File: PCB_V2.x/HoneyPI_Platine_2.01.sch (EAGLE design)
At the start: 69 parts

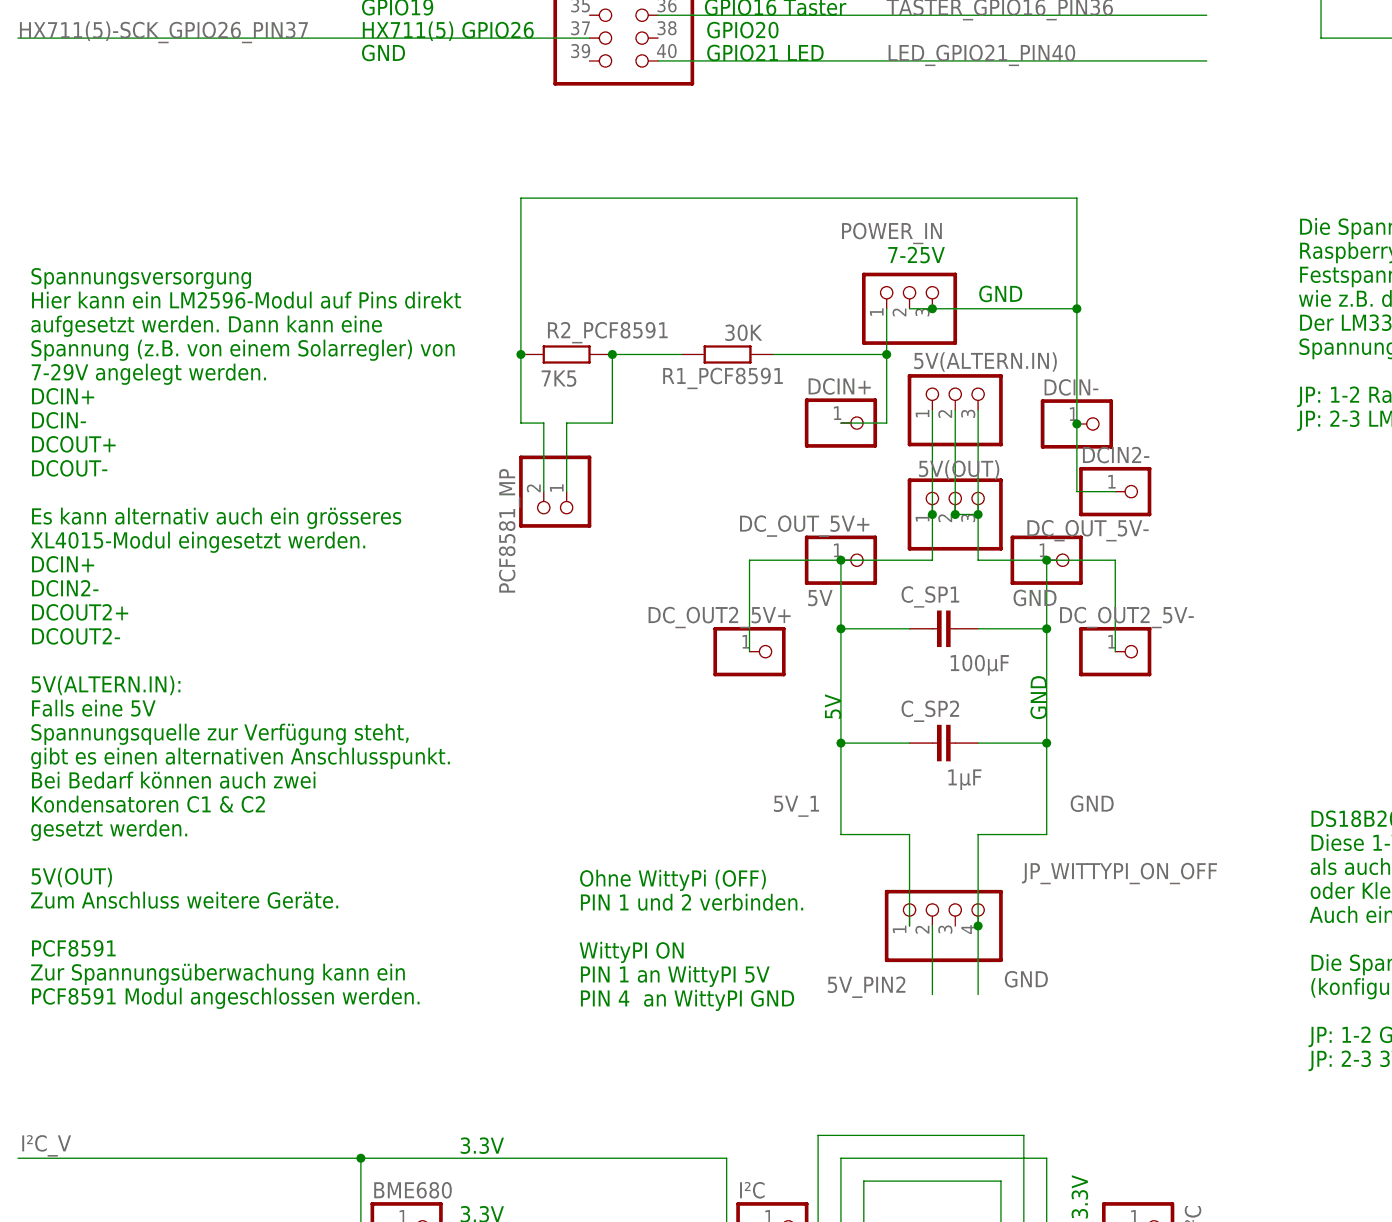
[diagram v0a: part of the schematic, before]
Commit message: 2x Polyfuse
The circuit has been extended by 2 optional polyfuses or similar.  The fuse size has been accepted and not yet verified.
Please note: The operator of the board must ensure safe operation. Accordingly, a fuse must be installed in accordance with the regulations.
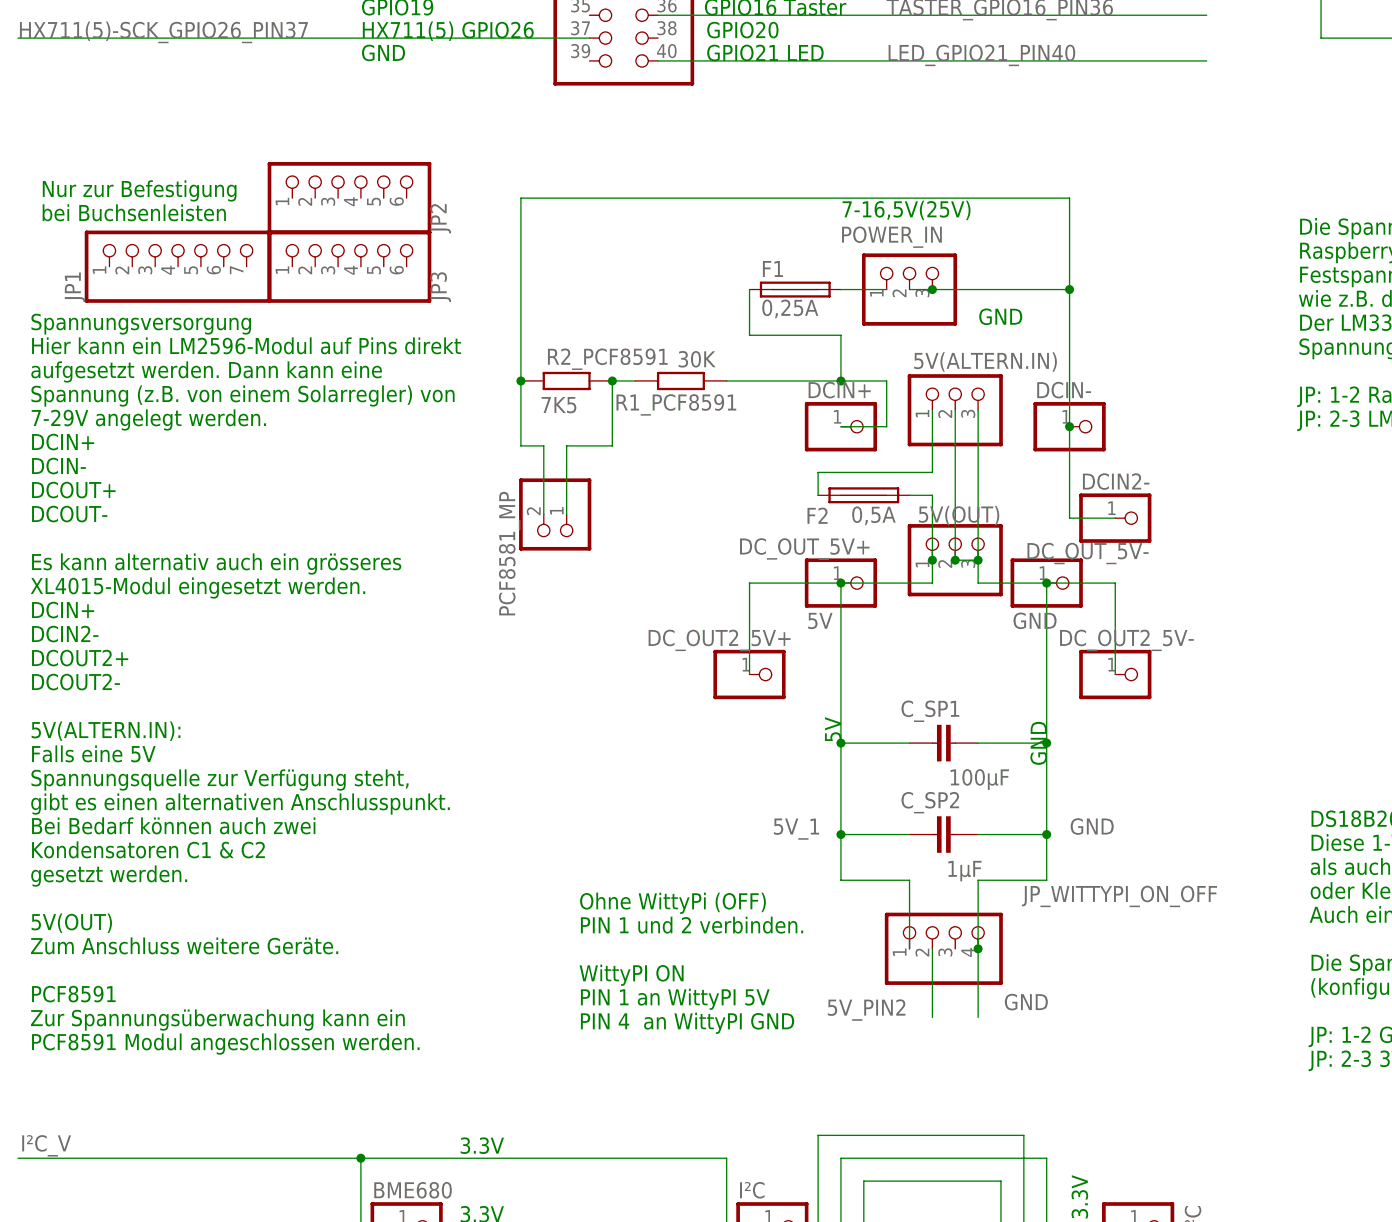
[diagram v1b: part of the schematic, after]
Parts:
- added F1: 0,25A, fuse:TR5
- added F2: 0,5A, fuse:TR5
- added JP1: (no value), pinhead:PINHD-1X7
- added JP2, JP3: (no value), pinhead:PINHD-1X6
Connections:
- removed net N$45: DCIN+.1, POWER_IN.1, R1_PCF8591.1
- new net N$5: DCIN+.1, F1.1, R1_PCF8591.1
- new net N$7: F1.2, POWER_IN.1
- new net N$9: 5V(ALTERN.IN).1, F2.2
- net 5V_1: now also F2.1; no longer 5V(ALTERN.IN).1
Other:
- note added: "7-16,5V(25V)"
- note added: "Nur zur Befestigung bei Buchsenleisten"
- note removed: "7-25V"
- moved on the sheet: 5V(OUT), C_SP1, C_SP2, DCIN-, DCIN2-, DC_OUT2_5V+, DC_OUT2_5V-, DC_OUT_5V+, DC_OUT_5V-, JP_WITTYPI_ON_OFF, PCF8581_MP, POWER_IN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
